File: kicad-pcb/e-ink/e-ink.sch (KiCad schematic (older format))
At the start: 22 parts

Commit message: added VCOM conditioner
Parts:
- removed L?: 22uH, symbol Device:L
- removed U?: LM79L15_TO92, Package_TO_SOT_THT:TO-92_Inline, symbol Regulator_Linear:LM79L15_TO92
- added C? (x2): 1uF, Capacitor_SMD:C_0402_1005Metric, symbol Device:C
- added C? (x5): 0.1uF, Capacitor_SMD:C_0402_1005Metric, symbol Device:C
- added R?: 14k, Resistor_SMD:R_0402_1005Metric, symbol Device:R_US
- added R?: 100k, Resistor_SMD:R_0402_1005Metric, symbol Device:R_US
- added R? (x4): 0, Resistor_SMD:R_0402_1005Metric, symbol Device:R_US
- added R?: 28k, Resistor_SMD:R_0402_1005Metric, symbol Device:R_US
- added R?: 80.6K, Resistor_SMD:R_0402_1005Metric, symbol Device:R_US
- added TP? (x2): TestPoint, symbol Connector:TestPoint
- added U?: LM78L15ACM_NOPB, symbol custom:LM78L15ACM_NOPB
- added U?: LM79L15ACM_NOPB, symbol custom:LM79L15ACM_NOPB
- added U?: STVM100DS6F, symbol custom:STVM100DS6F
- added U? (x3): TS512BIYDT, symbol custom:TS512BIYDT
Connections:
- net labels added: +15V, -15V, 3.3V, VCOM+, VCOM-, VCOM_BUF
- wire segments 62 -> 147
- no-connect marks 0 -> 3
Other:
- moved on the sheet: C?

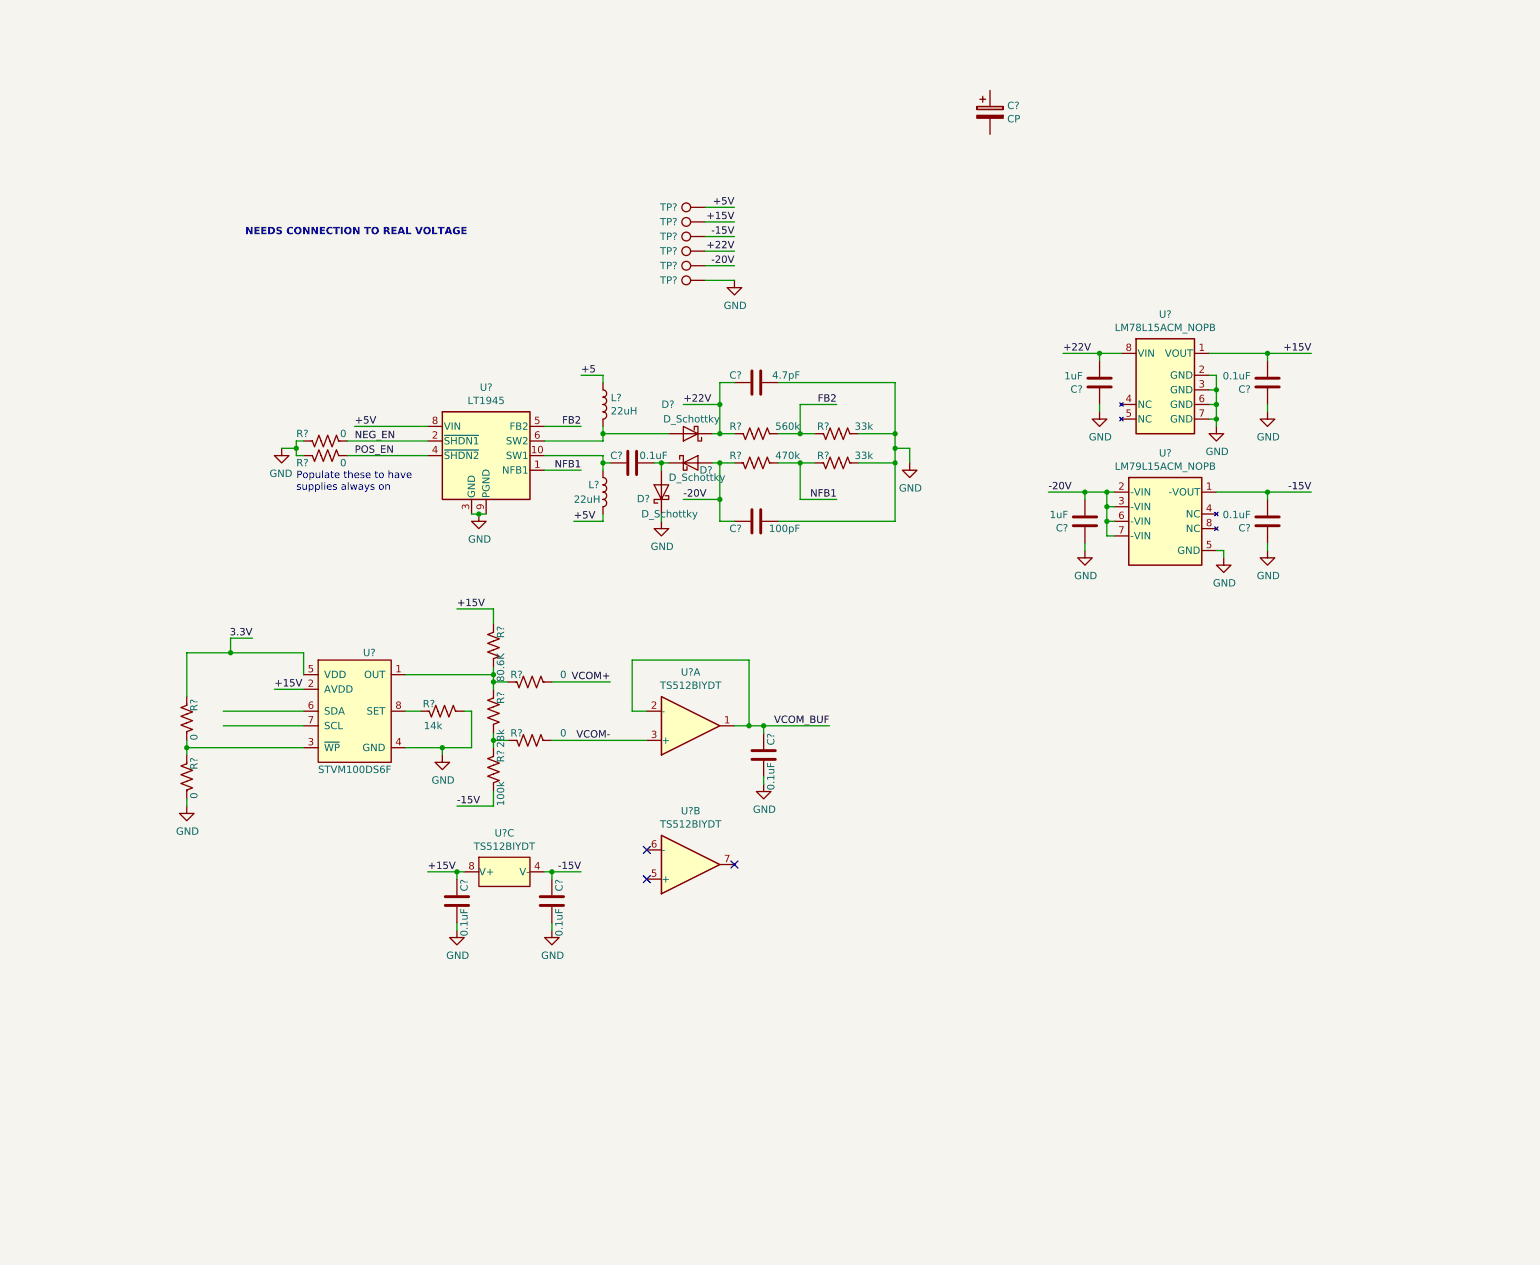
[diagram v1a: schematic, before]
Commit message: added 3.3v buck and annotations. PSUs done
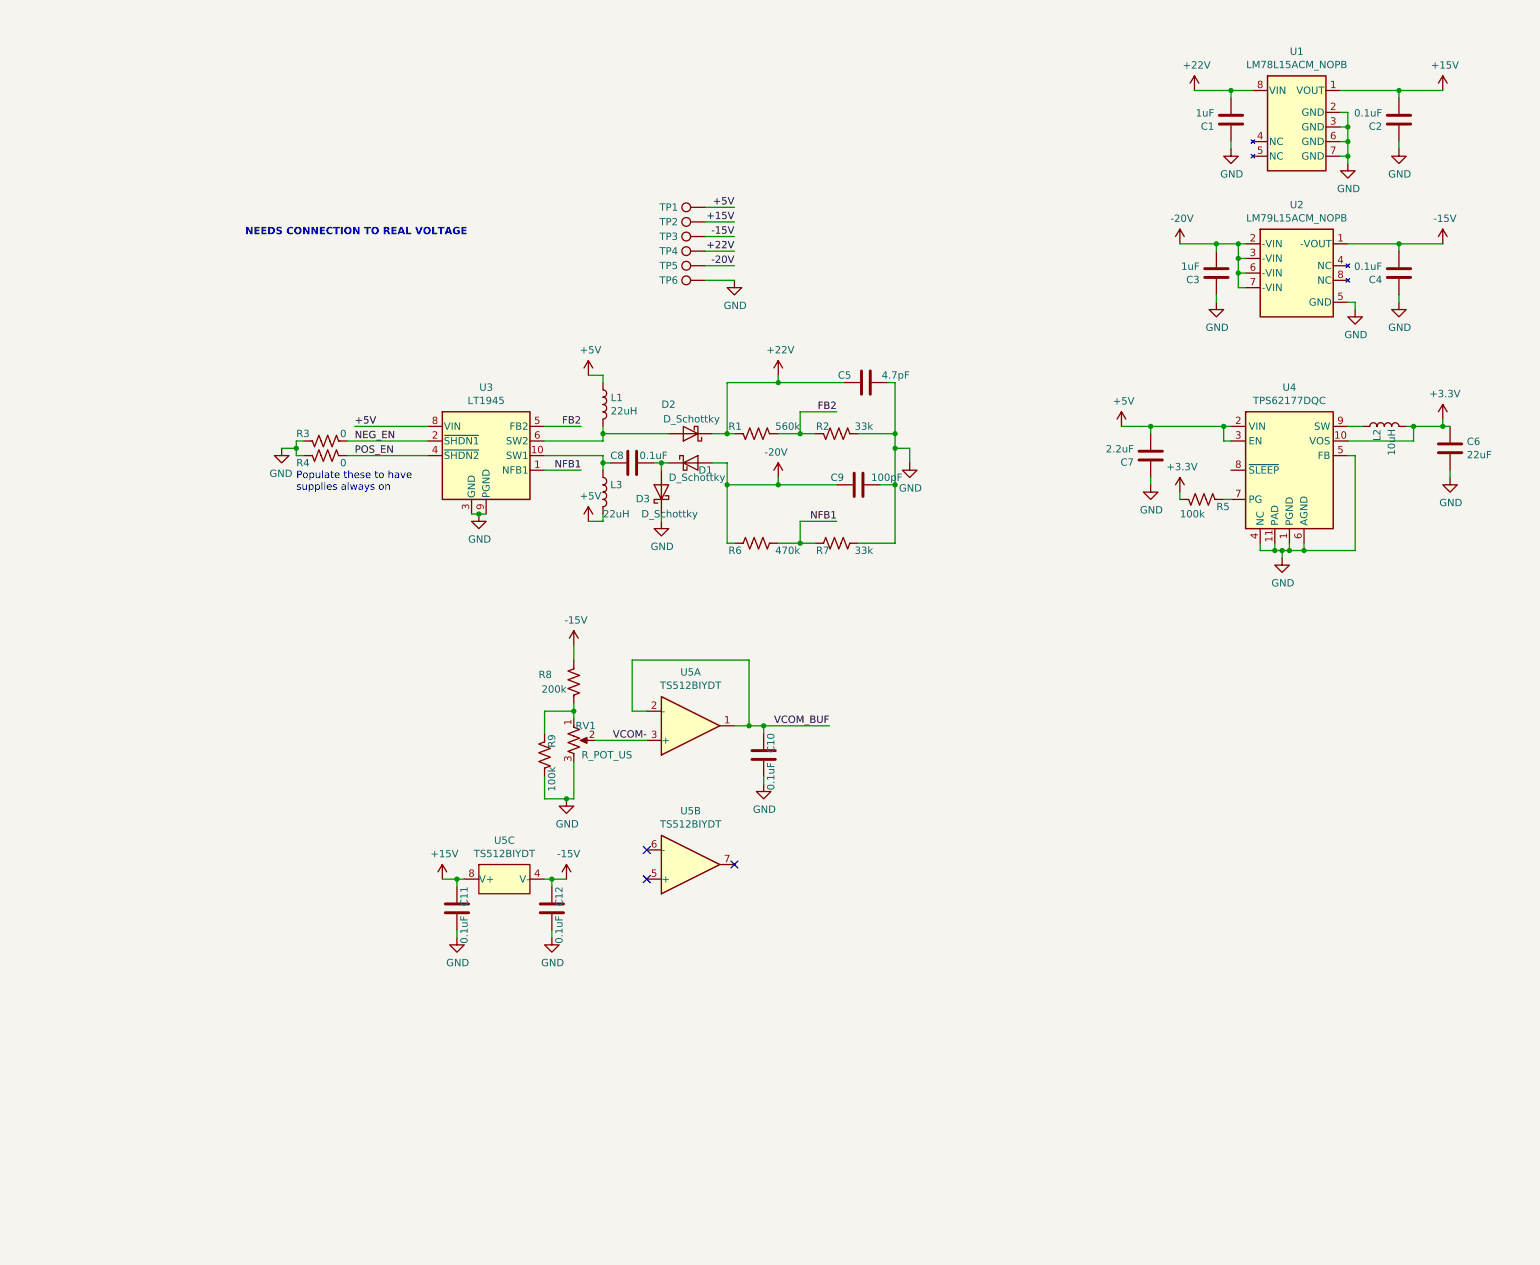
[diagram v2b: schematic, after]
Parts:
- removed C?: CP, symbol Device:CP
- removed R?: 14k, Resistor_SMD:R_0402_1005Metric, symbol Device:R_US
- removed R? (x4): 0, Resistor_SMD:R_0402_1005Metric, symbol Device:R_US
- removed R?: 28k, Resistor_SMD:R_0402_1005Metric, symbol Device:R_US
- removed U?: STVM100DS6F, symbol custom:STVM100DS6F
- added C6: 22uF, Capacitor_SMD:C_0402_1005Metric, symbol Device:C
- added C7: 2.2uF, Capacitor_SMD:C_0402_1005Metric, symbol Device:C
- added L2: 10uH, symbol Device:L
- added R5: 100k, Resistor_SMD:R_0402_1005Metric, symbol Device:R_US
- added RV1: R_POT_US, symbol Device:R_POT_US
- added U4: TPS62177DQC, Package_SON:WSON-10-1EP_2x3mm_P0.5mm_EP0.84x2.4mm_ThermalVias, symbol Regulator_Switching:TPS62177DQC
- R8: renamed from R?; value 80.6K -> 200k
- gave numbers to parts that had none: 32
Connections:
- net +5 is gone; now on net +5V: L1.1
- net +15V: no longer R8.1
- net +5V: now also C7.2, U4.2 (VIN), U4.3 (EN)
- net -15V: now also R8.1; no longer R9.2
- net GND: now also R9.2, C6.2, C7.1, RV1.3, U4.1 (PGND), U4.11 (PAD), U4.4 (NC), U4.5 (FB), U4.6 (AGND)
- net VCOM-: now also RV1.2
- net at R8.2: now also R9.1, RV1.1
- new net: L2.1, U4.9 (SW)
- new net: R5.1, U4.7 (PG)
- new net +3V3: C6.1, L2.2, R5.2, U4.10 (VOS)
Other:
- moved on the sheet: C1, C11, C12, C2, C3, C4, C5, C9, R6, R7, R8, R9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

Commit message: reorganized schems and added a note about buffer
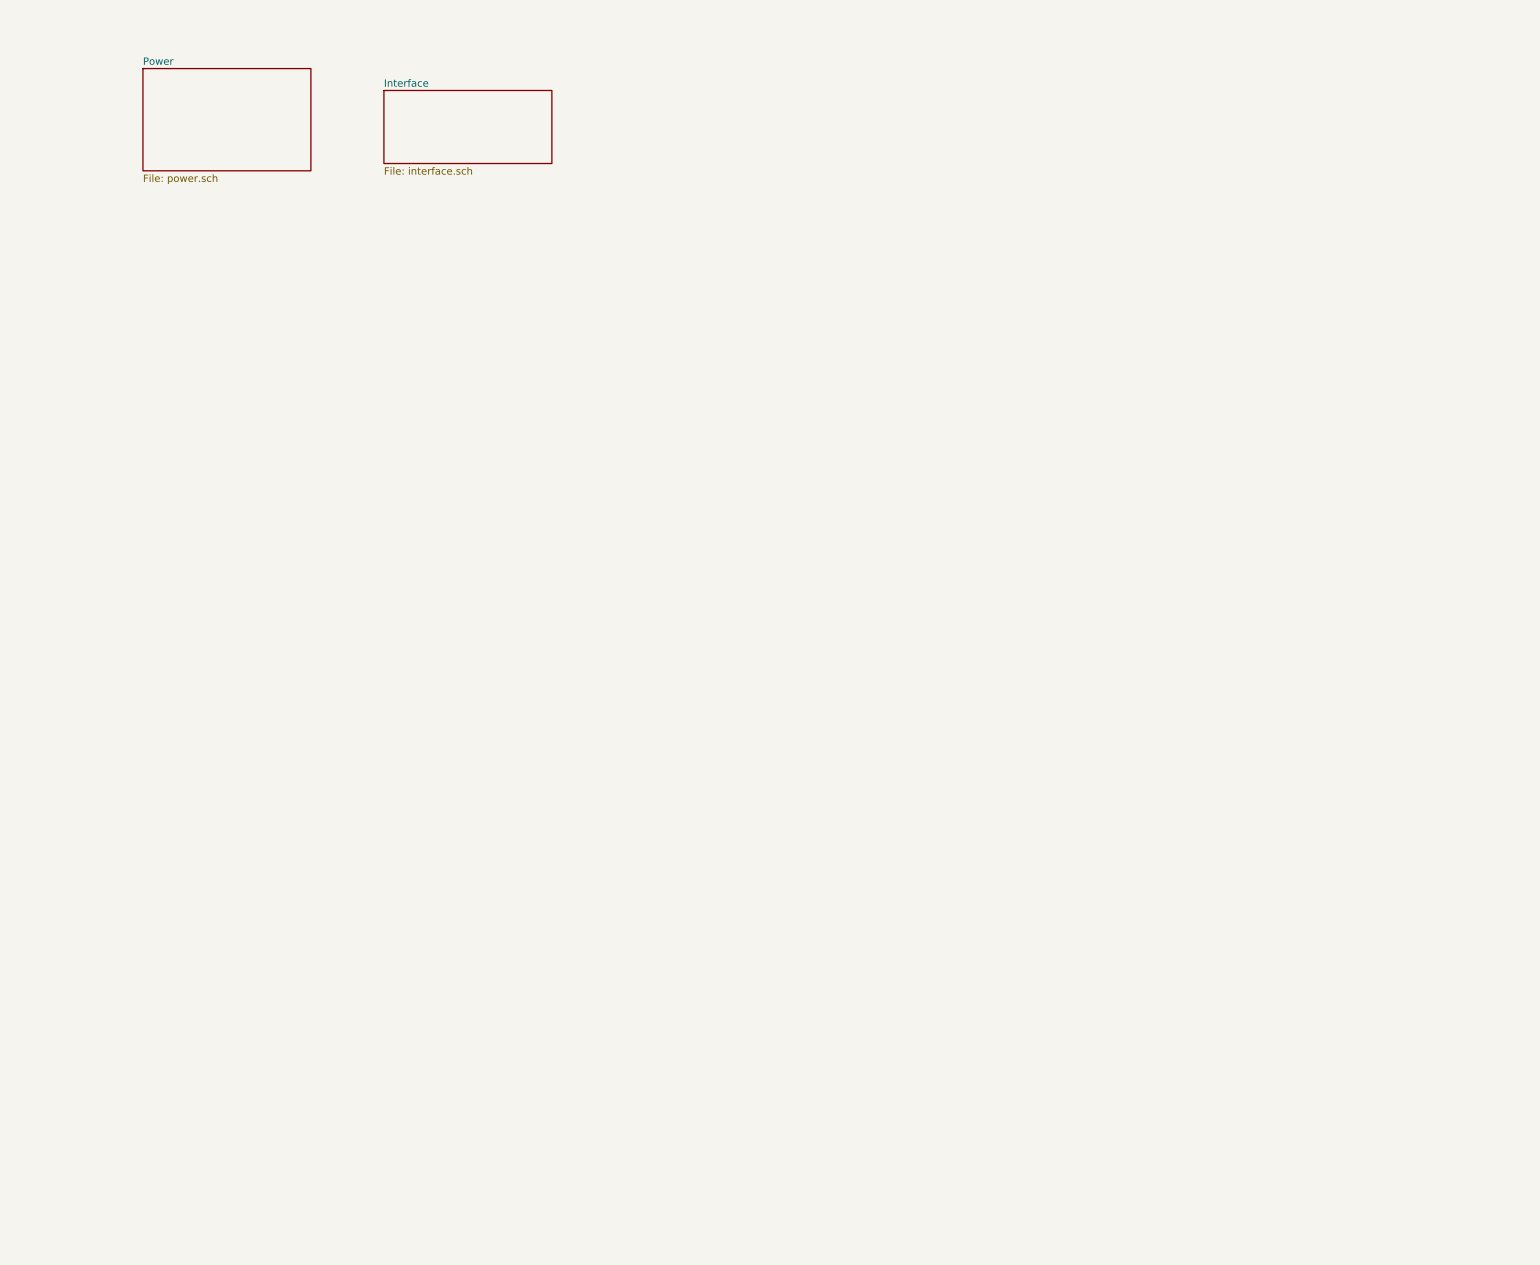
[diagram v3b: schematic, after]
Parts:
- removed C1, C3: 1uF, Capacitor_SMD:C_0402_1005Metric, symbol Device:C
- removed C10, C11, C12, C2, C4, C8: 0.1uF, Capacitor_SMD:C_0402_1005Metric, symbol Device:C
- removed C5: 4.7pF, Capacitor_SMD:C_0402_1005Metric, symbol Device:C
- removed C6: 22uF, Capacitor_SMD:C_0402_1005Metric, symbol Device:C
- removed C7: 2.2uF, Capacitor_SMD:C_0402_1005Metric, symbol Device:C
- removed C9: 100pF, Capacitor_SMD:C_0402_1005Metric, symbol Device:C
- removed D1, D2, D3: D_Schottky, symbol Device:D_Schottky
- removed L1, L3: 22uH, symbol Device:L
- removed L2: 10uH, symbol Device:L
- removed R1: 560k, Resistor_SMD:R_0402_1005Metric, symbol Device:R_US
- removed R2, R7: 33k, Resistor_SMD:R_0402_1005Metric, symbol Device:R_US
- removed R3, R4: 0, Resistor_SMD:R_0402_1005Metric, symbol Device:R_US
- removed R5, R9: 100k, Resistor_SMD:R_0402_1005Metric, symbol Device:R_US
- removed R6: 470k, Resistor_SMD:R_0402_1005Metric, symbol Device:R_US
- removed R8: 200k, Resistor_SMD:R_0402_1005Metric, symbol Device:R_US
- removed RV1: R_POT_US, symbol Device:R_POT_US
- removed TP1, TP2, TP3, TP4, TP5, TP6: TestPoint, symbol Connector:TestPoint
- removed U1: LM78L15ACM_NOPB, symbol custom:LM78L15ACM_NOPB
- removed U2: LM79L15ACM_NOPB, symbol custom:LM79L15ACM_NOPB
- removed U3: LT1945, Package_SO:MSOP-10_3x3mm_P0.5mm, symbol Regulator_Switching:LT1945
- removed U4: TPS62177DQC, Package_SON:WSON-10-1EP_2x3mm_P0.5mm_EP0.84x2.4mm_ThermalVias, symbol Regulator_Switching:TPS62177DQC
- removed U5: TS512BIYDT, symbol custom:TS512BIYDT
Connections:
- no-connect marks 3 -> 0
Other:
- note removed: "NEEDS CONNECTION TO REAL VOLTAGE"
- note removed: "Populate these to have\nsupplies always on"

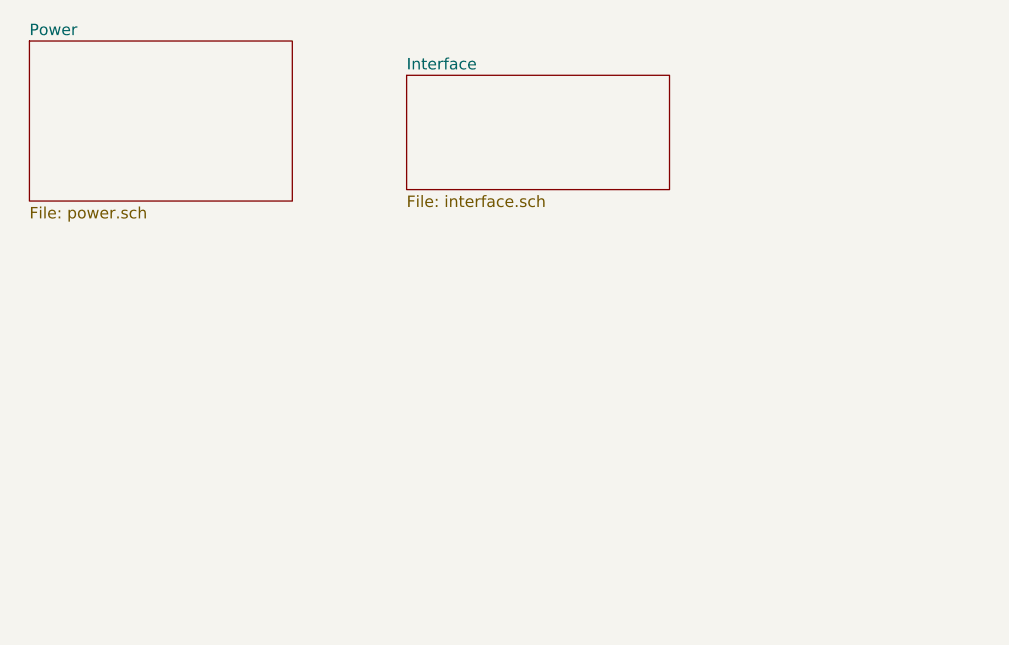
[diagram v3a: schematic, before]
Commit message: I think the schematic is done. ugly but feature-complete
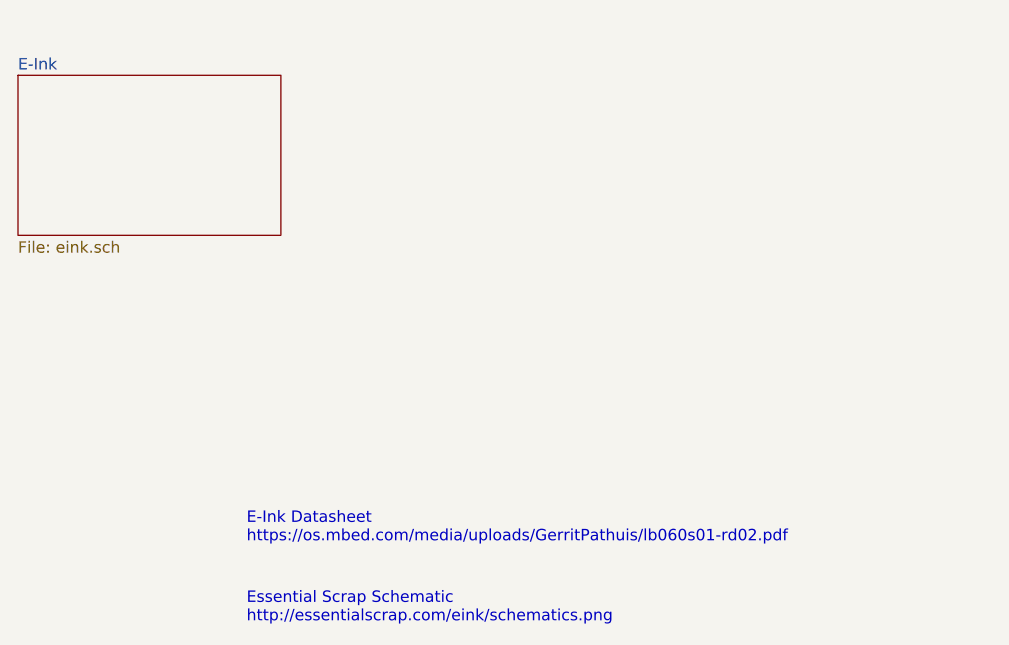
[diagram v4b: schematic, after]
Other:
- note added: "E-Ink Datasheet\nhttps://os.mbed.com/media/uploads/GerritPathuis/lb060s01-rd02.pdf"
- note added: "Essential Scrap Schematic\nhttp://essentialscrap.com/eink/schematics.png"
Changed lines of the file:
@@
 EESchema Schematic File Version 4
 LIBS:e-ink-cache
-EELAYER 26 0
+EELAYER 30 0
 EELAYER END
 $Descr USLetter 11000 8500
 encoding utf-8
-Sheet 1 3
+Sheet 1 2
 Title "E-Ink Bullshit"
 Date "2019-02-03"
@@
 $EndDescr
 $Sheet
-S 1400 950  1150 700
+S 1350 1100 1150 700
 U 5C57D13E
-F0 "Power" 50
-F1 "power.sch" 50
+F0 "E-Ink" 50
+F1 "eink.sch" 50
 $EndSheet
-$Sheet
-S 3050 1100 1150 500
-U 5C5A66EB
-F0 "Interface" 50
-F1 "interface.sch" 50
-$EndSheet
+Text Notes 2350 3150 0    50   ~ 0
+E-Ink Datasheet\nhttps://os.mbed.com/media/uploads/GerritPathuis/lb060s01-rd02.pdf
+Text Notes 2350 3500 0    50   ~ 0
+Essential Scrap Schematic\nhttp://essentialscrap.com/eink/schematics.png
 $EndSCHEMATC
